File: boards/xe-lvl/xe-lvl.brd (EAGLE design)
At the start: 100 x 50 mm, 67 parts, among them IC1 STM32MP157AAA3, IC2 MT41K256M16TW-107_P, IC3 STPMIC1APQR, J1 DCJ0202

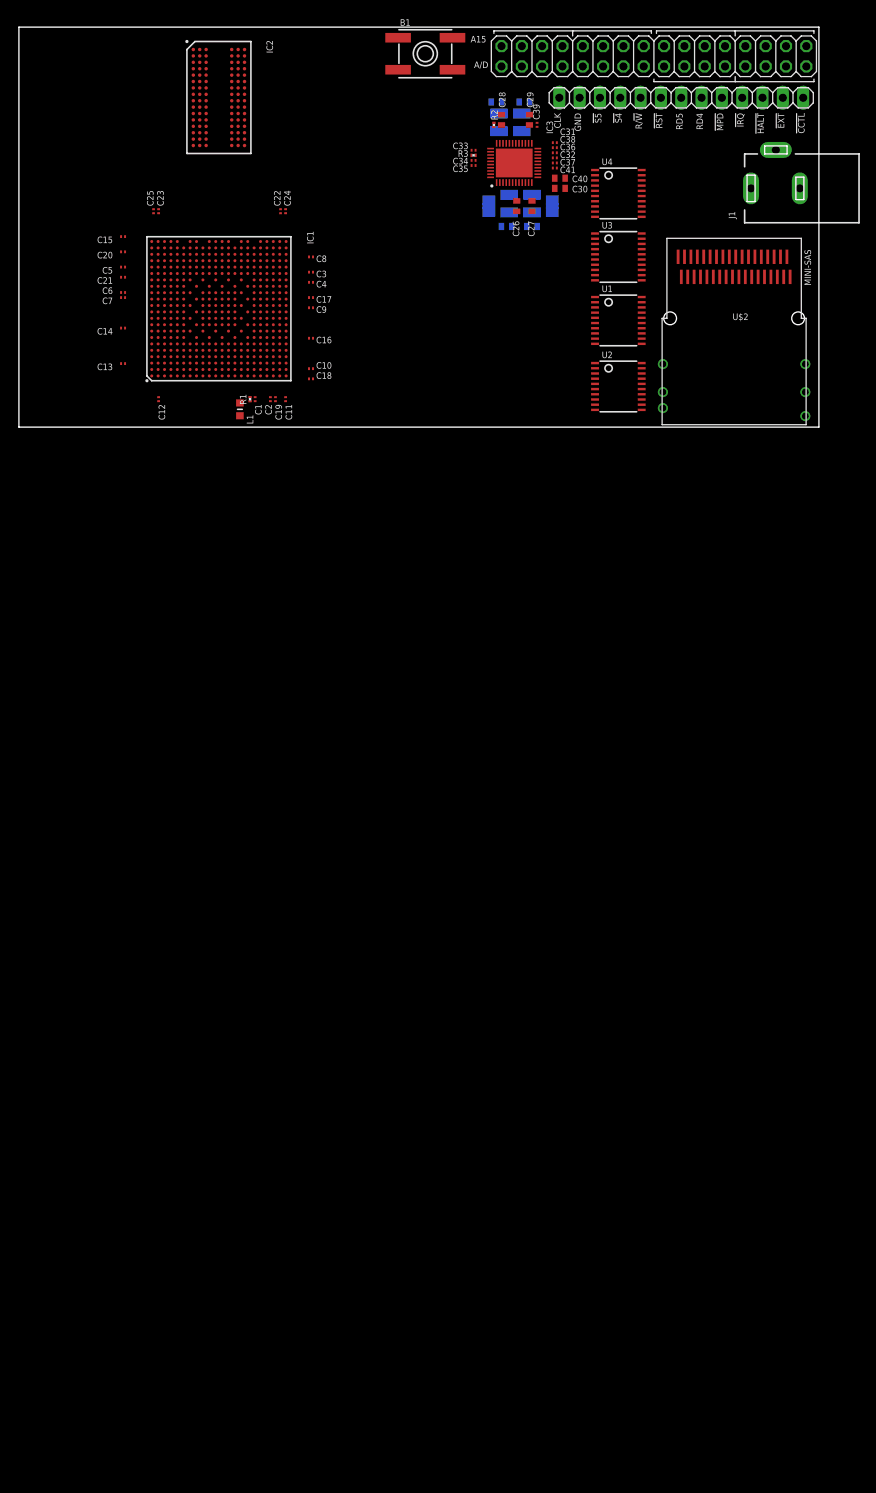
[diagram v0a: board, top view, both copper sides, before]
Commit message: Get the power and DDR parts sorted out. Still needs layout on the DDR.
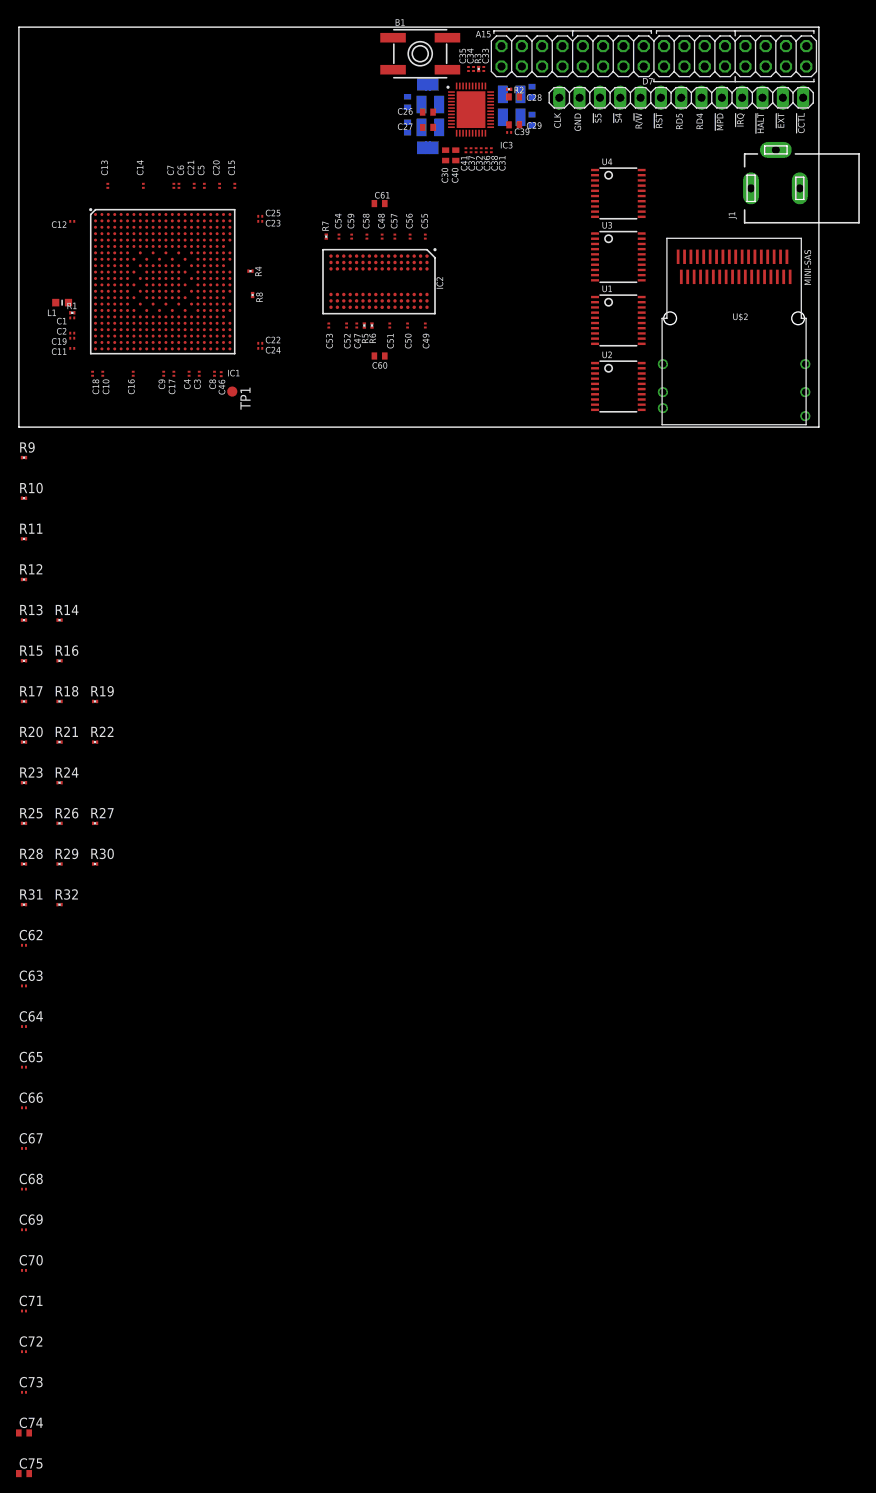
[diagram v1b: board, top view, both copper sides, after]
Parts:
- added C46, C47, C48, C49, C50, C51, C52, C53, C54, C55, C56, C57, C58, C59, C62, C63, C64, C65, C66, C67, C68, C69, C70, C71, C72, C73: 100nF, rcl:C0201
- added C60, C61: 10uF, rcl:C0402
- added C74, C75: 22uF, rcl:C0402
- added R10, R11, R12, R13, R14, R15, R16, R17, R18, R19, R20, R21, R22, R23, R24, R25, R26, R27, R28, R29, R30, R31, R32, R9: 56R, rcl:R0201
- added R4, R5: 240R, rcl:R0201
- added R6, R7: 10K, rcl:R0201
- added R8: 100R, rcl:R0201
- added TP1: TPB1,27, testpad:B1,27
- IC2: value MT41K256M16TW-107_P -> IS43TR16256B-125KBL
- moved IC2 30.5 mm to (45.0, 18.2), turned to 270 degrees
- moved C11 27.4 mm to (6.67, 9.84), turned to 180 degrees
- moved C18 27.3 mm to (9.21, 6.67), turned to 270 degrees
- moved C19 26.5 mm to (6.67, 11.1), turned to 180 degrees
- moved C2 26.1 mm to (6.67, 11.7), turned to 180 degrees
- moved C10 26.0 mm to (10.5, 6.67), turned to 270 degrees
- moved L1 25.9 mm to (5.40, 15.6), turned to 0 degrees
- moved C1 25.0 mm to (6.67, 13.7), turned to 180 degrees
- moved C12 24.7 mm to (6.67, 25.7), turned to 180 degrees
- moved R1 24.7 mm to (6.67, 14.3), turned to 180 degrees
- moved C16 22.7 mm to (14.3, 6.67), turned to 270 degrees
- moved C13 22.3 mm to (11.1, 30.2), turned to 90 degrees
- moved C9 20.2 mm to (18.1, 6.67), turned to 270 degrees
- moved C44 19.9 mm to (48.6, 37.5), turned to 90 degrees
- moved C45 19.9 mm to (48.6, 40.6), turned to 270 degrees
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- renumbered A/D to D7
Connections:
- new net N$15: IC1.K22, R4.1
- new net N$16: IC1.AA19, TP1.TP
- new net N$17: IC2.L8, R5.1
- net !DDR_CAS!: now also R28.1
- net !DDR_CS!: now also R29.1
- net !DDR_RAS!: now also R27.1
- net !DDR_RESET!: now also R7.2
- net !DDR_WE!: now also R31.1
- net +5V: now also J1.1
- net DDR_A0: now also R9.1
- net DDR_A1: now also R10.1
- net DDR_A10: now also R19.1
- net DDR_A11: now also R20.1
- net DDR_A12: now also R21.1
- net DDR_A13: now also R22.1
- net DDR_A14: now also R23.1
- net DDR_A2: now also R11.1
- net DDR_A3: now also R12.1
- net DDR_A4: now also R13.1
- net DDR_A5: now also R14.1
- net DDR_A6: now also R15.1
- net DDR_A7: now also R16.1
- net DDR_A8: now also R17.1
- net DDR_A9: now also R18.1
- net DDR_BA0: now also R24.1
- net DDR_BA1: now also R25.1
- net DDR_BA2: now also R26.1
- net DDR_CKE: now also R30.1, R6.2
- net DDR_CK_N: now also R8.2
- net DDR_CK_P: now also R8.1
- net DDR_ODT: now also R32.1
- net GND: now also C46.2, C47.1, C48.1, C49.1, C50.1, C51.1, C52.1, C53.1, C54.1, C55.1, C56.1, C57.1, C58.1, C59.1, C60.2, C61.2, C62.1, C63.1, C64.1, C65.1, C66.1, C67.1, C68.1, C69.1, C70.1, C71.1, C72.1, C73.1, C74.1, C75.1, J1.2, J1.3, R4.2, R5.2, R6.1, R7.1
- net VDD_DDR: now also C49.2, C50.2, C51.2, C52.2, C53.2, C54.2, C55.2, C56.2, C57.2, C58.2, C59.2, C60.1, C61.1
- net VREF_DDR: now also C46.1, C47.2, C48.2, IC1.AB19, IC2.H1, IC2.M8
- net VTT_DDR: now also C62.2, C63.2, C64.2, C65.2, C66.2, C67.2, C68.2, C69.2, C70.2, C71.2, C72.2, C73.2, C74.2, C75.2, R10.2, R11.2, R12.2, R13.2, R14.2, R15.2, R16.2, R17.2, R18.2, R19.2, R20.2, R21.2, R22.2, R23.2, R24.2, R25.2, R26.2, R27.2, R28.2, R29.2, R30.2, R31.2, R32.2, R9.2
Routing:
- removed copper zone on layer 15, net DDR_CORE

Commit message: Started on capacitor/terminator layout for the DDR
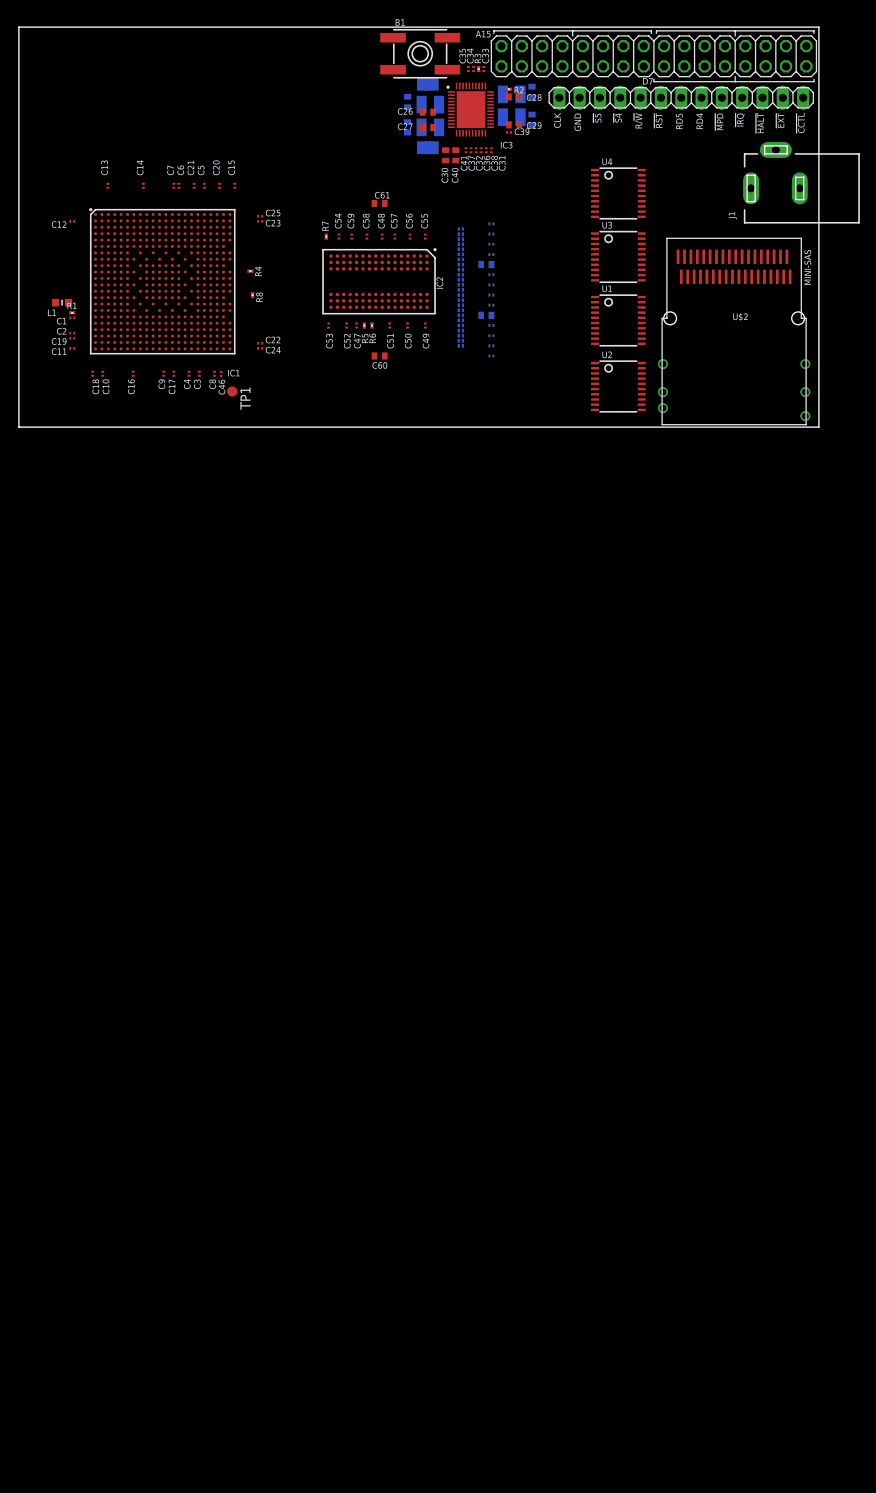
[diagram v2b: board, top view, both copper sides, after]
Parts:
- moved C74 157.1 mm to (58.4, 20.3), flipped to the bottom
- moved C75 155.9 mm to (58.4, 14.0), flipped to the bottom
- moved C73 143.3 mm to (59.1, 10.2), flipped to the bottom
- moved C72 139.8 mm to (59.1, 11.4), flipped to the bottom
- moved C69 138.6 mm to (59.1, 25.4), flipped to the bottom
- moved C71 136.3 mm to (59.1, 12.7), flipped to the bottom
- moved C70 134.0 mm to (59.1, 15.2), flipped to the bottom
- moved C67 121.6 mm to (59.1, 16.5), flipped to the bottom
- moved C68 119.4 mm to (59.1, 8.89), flipped to the bottom
- moved C66 118.3 mm to (59.1, 17.8), flipped to the bottom
- moved C65 115.0 mm to (59.1, 19.1), flipped to the bottom
- moved C64 112.8 mm to (59.1, 21.6), flipped to the bottom
- moved C63 109.6 mm to (59.1, 22.9), flipped to the bottom
- moved C62 106.4 mm to (59.1, 24.1), flipped to the bottom
- moved R31 89.2 mm to (55.2, 10.8), flipped to the bottom
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
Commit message: Latest layout
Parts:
- moved R32 15.2 mm to (55.2, 25.4), turned to 180 degrees
- moved R29 12.1 mm to (55.2, 24.1), turned to 180 degrees
- moved R31 9.53 mm to (55.2, 20.3), turned to 180 degrees
- moved R10 9.52 mm to (55.2, 14.6), turned to 180 degrees
- moved R28 9.52 mm to (55.2, 21.0), turned to 180 degrees
- moved R15 8.26 mm to (55.2, 12.1), turned to 180 degrees
- moved R13 8.25 mm to (55.2, 13.3), turned to 180 degrees
- moved R17 8.25 mm to (55.2, 11.4), turned to 180 degrees
- moved R24 6.35 mm to (55.2, 21.6), turned to 180 degrees
- moved R27 6.35 mm to (55.2, 19.7), turned to 180 degrees
- moved R16 5.08 mm to (55.2, 26.0), turned to 180 degrees
- moved R20 5.08 mm to (55.2, 14.0), turned to 180 degrees
- moved R26 5.08 mm to (55.2, 19.1), turned to 180 degrees
- moved R19 1.91 mm to (55.2, 15.9), turned to 180 degrees
- moved C74 1.80 mm to (59.7, 21.6)
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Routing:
- added copper zone on layer 15, net VTT_DDR
